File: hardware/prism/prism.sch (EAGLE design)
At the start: 136 parts, among them IC1 MAX3232CSE, IC2 XMEGA128-A1, IC3 LM1086CS-3.3, J1 1445055-2, J2 2MS1T2B4M6QNS, K1 LED_G, K2 LED_G, K3 LED_G, K4 LED_G, K5 LED_G, K6 LED_G, K7 LED_G, K8 LED_G, T1 FDFS2P753Z, T2 MMBT2222LT1G, T3 MMBT2222LT1G, T4 FDFS2P753Z, T5 MMBT2222LT1G, T6 MMBT2222LT1G, T7 FDFS2P753Z, T8 MMBT2222LT1G

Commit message: add 3,3v and 5v regulator
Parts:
- added C30: 1µF 25V, robotter_capacitor:1UFD_25V
- added C31: 10nF 50V, robotter_capacitor:10NF-F
- added C32: 100nF 50V, robotter_capacitor:100NF-F
- added C33, C34: 10µF 25V, robotter_capacitor:10UF-C_25V
- added D8: B160-13F, robotter_diode:B160-13F
- added IC4: LM25011MY, robotter_ic:LM25011MY
- added L1: SDR0805-270KL, robotter_inductor:SDR0805-270KL
- added R58: 75K-F, robotter_resistor:75K-F
- added R59: 100_1W-1W, robotter_resistor:100_1W-1W
- added R60: 10K-F, robotter_resistor:10K-F
- added R61: 3K09-F, robotter_resistor:3K09-F
- C19, C23, C25, C26: device rcl:C-EUC0805 -> robotter_capacitor:100NF-F
- C21: value C_10UF -> 10µF 25V; device robotter_capacitor:C_10UF -> robotter_capacitor:10UF-C_25V
- C22: value C_10UF -> 1µF 25V; device robotter_capacitor:C_10UF -> robotter_capacitor:1UFD_25V
- C28: value 10UFC -> 10UF-C_25V; device robotter_capacitor:10UFC -> robotter_capacitor:10UF-C_25V
- D7: value 50WQ03 -> (none)
- IC3: value LM1086CS-3.3 -> NCV78M05BDTRKG; device robotter_ic:LM1086CS-3.3 -> linear:NCV78M05BDTRKG
- R14: device robotter_resistor:RES_1K -> robotter_resistor:RES_2K2
- R22: value RES_0 -> 0.27-F; device robotter_resistor:RES_0 -> robotter_resistor:0.27-F
- R27, R31, R38, R45: device rcl:R-EU_R0603 -> robotter_resistor:1K-F
- RF: value YELLOW_0805 -> YELLOW
- T2, T3, T5, T6, T8: device transistor-neu-to92:MMBT2222ALT1-NPN-SOT23-BEC -> robotter_ic:MMBT2222ALT1-NPN-SOT23-BEC
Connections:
- removed net 3V3_BUS: R22.1
- new net N$38: C32.2, D8.C, IC4.SW, L1.1
- new net N$39: D8.A, IC4.CS, R22.2
- new net N$40: IC4.RT, R58.1
- new net N$41: C21.1, IC3.VI, R59.2
- new net N$43: C31.1, IC4.SS
- new net N$44: IC4.FB, R60.1, R61.2
- new net N$48: C32.1, IC4.BST
- net +3V3: now also C33.1, L1.2, R61.1; no longer C22.1, IC3.VOUT@0, IC3.VOUT@1, R22.2
- net +5V: now also C34.1, IC3.VO; no longer C21.1, IC3.VIN
- net GND: now also C30.2, C31.2, C33.2, C34.2, IC4.CSG, IC4.SGND, R22.1, R60.2
- net VBAT: now also C22.1, C30.1, IC4.VIN, R58.2, R59.1
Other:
- note removed: "manque regulo 5V"
- note removed: "vérifier puissance dissipée dans régulos"
- moved on the sheet: C21, C22, R22

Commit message: photointerrupter added to board, interfaces added, regulator added
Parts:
- removed D1, D4: bzv55-c3v3, diode:ZENER-DIODESOD80C
- removed MIRROR_IDX0, MIRROR_IDX1: 794681-4, con-amp:794681-4
- removed R19: nc, rcl:R-EU_R0603
- removed R20: 4k7, rcl:R-EU_R0805
- removed R36: nc, rcl:R-EU_R0805
- removed R47: 10k, rcl:R-EU_R0603
- removed T7: FDFS2P753Z, robotter:FDFS2P753Z
- added C35, C36, C37, C38, C39, C40: 100nF 50V, robotter_capacitor:100NF-F
- added IC5, IC6: 74LVC4245A, robotter_ic:74LVC4245A
- added PH1, PH2: GP1S58VJ000F, robotter_ic:GP1S58VJ000F
- added R62, R63: 10K-F, robotter_resistor:10K-F
- added R64: 4K7-E, robotter_resistor:4K7-E
- added R65, R66, R67, R68, R69, R70, R71: 0-F, robotter_resistor:0-F
- added T9: NTGS4111PT1G, robotter_ic:NTGS4111PT1G
- C1, C10, C11, C12, C13, C14, C15, C16, C3, C4, C5, C6, C7, C9: value C_10UF -> 100nF 50V; device robotter_capacitor:C_10UF -> robotter_capacitor:100NF-F
- C17, C18: value C_10UF -> 15pF_0603_100V; device robotter_capacitor:C_10UF -> robotter_capacitor:15PF-F
- C19, C23, C25, C26: value 100nF -> 100nF 50V
- C2: value 330UF_35V_G_EEEFK1V331P -> 330µF 35V; device robotter_capacitor:C_POL_330UF -> robotter_capacitor:330UF
- C20, C24: value 100nF -> 100nF 50V; device rcl:C-EUC0603 -> robotter_capacitor:100NF-F
- C27: value 10uF_35V_TANTALE -> 10µF 25V; device robotter_capacitor:C_POL_10UF -> robotter_capacitor:10UF-C_25V
- C28: value 10UF-C_25V -> 10µF 25V
- C29: value 100nF_0603_50V -> 100nF 50V
- C8: value C_10UF -> 10µF 25V; device robotter_capacitor:C_10UF -> robotter_capacitor:10UF-C_25V
- D2, D5: device diode:ZENER-DIODESOD80C -> robotter_diode:BZV55-C3V3SOD80C
- D3, D6: device diode:CGRM4004-G -> robotter_diode:CGRM4004-G
- IR_SENSOR0, IR_SENSOR1: device con-amp:794681-4 -> robotter_connector:794681-4
- R1, R2, R48, R49, R5, R6, R7, R8: value RES_15K -> 270-F; device robotter_resistor:RES_15K -> robotter_resistor:270-F
- R12: value nc -> 4K7-F; device rcl:R-EU_R0603 -> robotter_resistor:4K7-F
- R13: value 15K_5P_0805 -> 15k 1%; device robotter_resistor:RES_15K -> robotter_resistor:15K-E
- R14: value 1K_5P_0805 -> 1k; device robotter_resistor:RES_2K2 -> robotter_resistor:1K-E
- R15, R23, R24, R26, R3, R30, R32, R35, R37, R39, R4, R40, R46, R51, R52: value 10k -> 10K-F; device rcl:R-EU_R0603 -> robotter_resistor:10K-F
- R16: value 10k -> 4K7-F; device rcl:R-EU_R0603 -> robotter_resistor:4K7-F
- R17: value 4k7 -> 270-F; device rcl:R-EU_R0805 -> robotter_resistor:270-F
- R18: value nc -> 270-F; device rcl:R-EU_R0805 -> robotter_resistor:270-F
- R43: value 4k7 -> 4K7-E; device rcl:R-EU_R0805 -> robotter_resistor:4K7-E
- R44: value 4k7 -> 0-F; device rcl:R-EU_R0805 -> robotter_resistor:0-F
- T1, T4: value FDFS2P753Z -> NTGS4111PT1G; device robotter:FDFS2P753Z -> robotter_ic:NTGS4111PT1G
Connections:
- removed net INT1_5V: BAL0.6
- removed net MIRROR_1_INDEX_3V3: D4.C, R12.2, R43.1
- removed net MIRROR_INDEX_0_24V: MIRROR_IDX0.2, R16.1, R17.2, R18.2
- removed net MIRROR_INDEX_1_24V: MIRROR_IDX1.2, R36.2, R37.1, R43.2
- new net INT0_0_3V3: IC6.IO_VL5, R71.1
- new net INT0_1_3V3: IC6.IO_VL4, R70.1
- new net INT1_0_3V3: IC6.IO_VL3, R69.1
- new net INT1_0_5V: BAL0.6, IC5.IO_VCC3, R65.2
- new net INT1_1_3V3: IC6.IO_VL2, R68.1
- new net MIRROR_INDEX_1_3V3: PH2.TRANSISTOR_C, R12.1
- new net N$47: IC6.IO_VCC2, R44.1
- new net N$49: IC5.IO_VL2, R68.2
- new net N$50: IC5.IO_VL4, R70.2
- new net N$51: IC5.IO_VL3, R69.2
- new net N$52: IC5.IO_VL5, R71.2
- new net N$53: IC6.IO_VCC3, R65.1
- new net N$54: IC6.IO_VCC5, R67.1
- new net N$55: IC6.IO_VCC4, R66.1
- new net N$56: PH2.LED_A, R18.1
- new net N$57: PH1.LED_A, R17.1
- new net SYNC_IN_0_3V3: IC5.IO_VL6
- new net SYNC_IN_1_3V3: IC5.IO_VL7
- new net SYNC_OUT_0_3V3: IC6.IO_VL6
- new net SYNC_OUT_1_3V3: IC6.IO_VL7
- net +3V3: now also C19.1, C26.1, C27.1, C35.1, C37.1, C39.1, C40.1, C6.1, IC5.DIR_H_TO_L, IC5.VL@0, IC5.VL@1, IC6.VL@0, IC6.VL@1, R12.2, R16.2, R17.2, R18.2, R62.1, R63.1; no longer C1.1, C27.+
- net +5V: now also C36.1, C38.1, IC5.VCC, IC6.VCC
- net GND: now also C17.2, C18.2, C27.2, C3.2, C35.2, C36.2, C37.2, C38.2, C39.2, C40.2, C6.2, IC5./OE, IC5.GND@0, IC5.GND@1, IC5.GND@2, IC6./OE, IC6.DIR_H_TO_L, IC6.GND@0, IC6.GND@1, IC6.GND@2, PH1.LED_C, PH1.TRANSISTOR_E, PH2.LED_C, PH2.TRANSISTOR_E, R35.1, R37.1; no longer C17.1, C18.1, C27.-, C4.2, C5.2, D1.A, D4.A, MIRROR_IDX0.1, MIRROR_IDX1.1, R12.1, R18.1, R19.1, R36.1, R46.1, R47.1
- net INT0_0_5V: now also IC5.IO_VCC5, R67.2
- net INT0_1_5V: now also IC5.IO_VCC4, R66.2
- net INT1_1_5V: now also IC5.IO_VCC2, R44.2
- net IR_SENSOR_0_OUTPUT_24V: now also R23.1, R64.1; no longer R20.2, R24.1
- net IR_SENSOR_0_OUTPUT_3V3: now also R64.2; no longer R20.1
- net IR_SENSOR_1_OUTPUT_24V: now also R39.1, R43.1; no longer R35.1, R44.2
- net IR_SENSOR_1_OUTPUT_3V3: now also R43.2; no longer R44.1
- net MIRROR_INDEX_0_3V3: now also PH1.TRANSISTOR_C, R16.1; no longer D1.C, R17.1, R19.2
- net MOTOR_PWM_1_3V3: now also R37.2; no longer R46.2
- net N$1: now also C5.1; no longer C3.1
- net N$11: now also C1.1; no longer C4.1
- net N$125: now also R23.2, T1.D@0, T1.D@1, T1.D@2, T1.D@3; no longer R24.2, T1.D, T1.D1
- net N$128: now also R24.1; no longer R23.1
- net N$13: now also C3.1; no longer C5.1
- net N$14: now also R46.1; no longer R39.1
- net N$24: now also C4.2; no longer C6.2
- net N$26: now also R51.2, R52.1, T9.G; no longer R51.1, R52.2, T7.G
- net N$29: now also R51.1; no longer R52.1
- net N$30: now also R52.2, T9.S; no longer R51.2, T7.S
- net N$45: now also C17.1; no longer C17.2
- net N$46: now also C18.1; no longer C18.2
- net N$5: now also C5.2; no longer C3.2
- net N$6: now also C4.1; no longer C6.1
- net N$8: now also C25.1, R39.2, T4.D@0, T4.D@1, T4.D@2, T4.D@3; no longer C24.1, R35.2, T4.D, T4.D1
- net ON/OFF_SENSOR_1_3V3: now also R35.2; no longer R47.2
- net RX_1_3V3: now also R62.2
- net SYNC_IN_0_5V: now also IC5.IO_VCC6
- net SYNC_IN_1_5V: now also IC5.IO_VCC7
- net SYNC_OUT_0_5V: now also IC6.IO_VCC6
- net SYNC_OUT_1_5V: now also IC6.IO_VCC7
- net TX_1_3V3: now also R63.2
- net VBAT: now also C24.1, R24.2, R46.2, T9.D@0, T9.D@1, T9.D@2, T9.D@3; no longer C19.1, C25.1, C26.1, MIRROR_IDX0.3, MIRROR_IDX1.3, R16.2, R23.2, R37.2, R39.2, T7.D, T7.D1
- net XBEE_CTS_3V3: now also IC2.PH2(!RAS!/ALE1)
- net XBEE_RTS_3V3: now also IC2.PH3(!DOM!/ALE2)
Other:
- note added: "3v3 -> 5v"
- note added: "3v3 <- 5v"
- moved on the sheet: BAL0, BAL1, C1, C10, C11, C12, C13, C14, C15, C16, C17, C18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

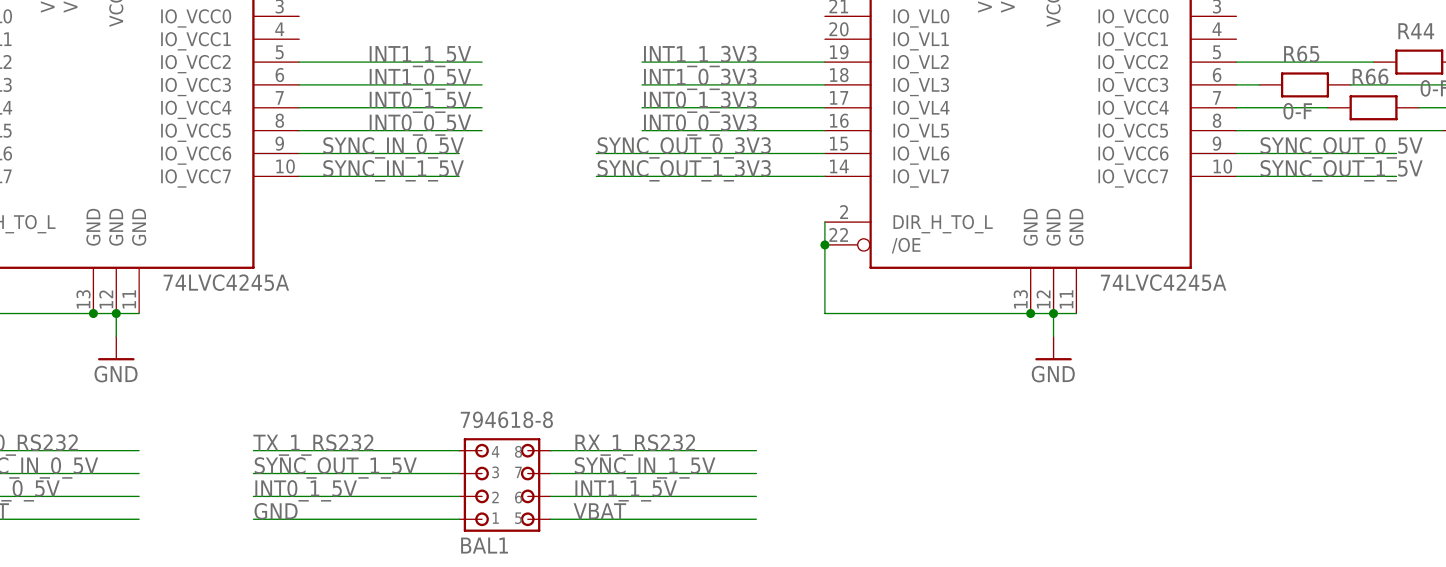
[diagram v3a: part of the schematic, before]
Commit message: prism/prism.brd
correction after Damien review
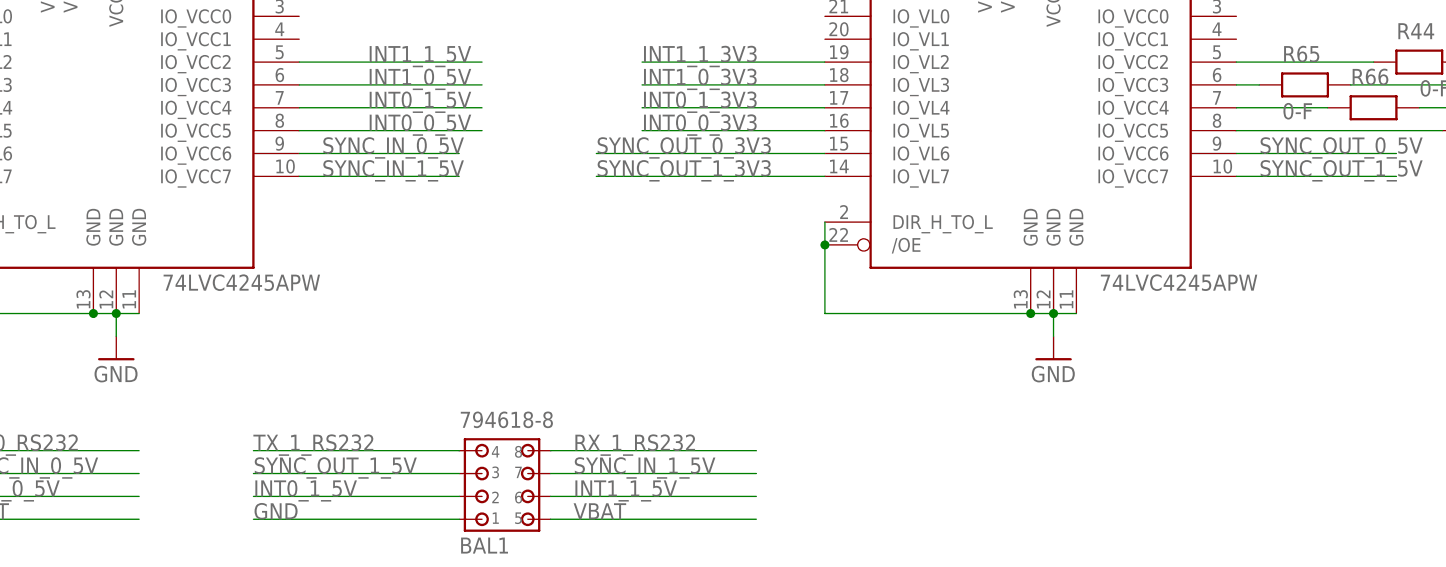
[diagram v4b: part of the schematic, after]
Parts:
- IC5, IC6: value 74LVC4245A -> 74LVC4245APW; device robotter_ic:74LVC4245A -> robotter_ic:74LVC4245APW
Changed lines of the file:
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@@
 <part name="R64" library="robotter_resistor" deviceset="4K7" device="-E"/>
 <part name="R43" library="robotter_resistor" deviceset="4K7" device="-E"/>
-<part name="IC6" library="robotter_ic" deviceset="74LVC4245" device="A"/>
+<part name="IC6" library="robotter_ic" deviceset="74LVC4245" device="APW"/>
 <part name="P+4" library="supply1" deviceset="+5V" device=""/>
 <part name="+3V5" library="supply1" deviceset="+3V3" device=""/>
@@
 <part name="R66" library="robotter_resistor" deviceset="0" device="-F"/>
 <part name="R67" library="robotter_resistor" deviceset="0" device="-F"/>
-<part name="IC5" library="robotter_ic" deviceset="74LVC4245" device="A"/>
+<part name="IC5" library="robotter_ic" deviceset="74LVC4245" device="APW"/>
 <part name="P+5" library="supply1" deviceset="+5V" device=""/>
 <part name="+3V7" library="supply1" deviceset="+3V3" device=""/>

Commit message: prism schematic modified, frist routing test
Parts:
- removed C26: 100nF 50V, robotter_capacitor:100NF-F
- removed H4: MOUNT-PAD-ROUND5.5, holes:MOUNT-PAD-ROUND5.5
- removed IR_SENSOR1: 794681-4, robotter_connector:794681-4
- removed PH2: GP1S58VJ000F, robotter_ic:GP1S58VJ000F
- removed R41: nc, rcl:R-EU_R0603
- removed R42: 0, rcl:R-EU_R0603
- removed R59: 100_1W-1W, robotter_resistor:100_1W-1W
- added C41: 180pF 50V, robotter_capacitor:180PF-F
- added C42, C43: 10µF 25V, robotter_capacitor:10UF-C_25V
- added D1: B120-13-F, robotter_diode:B120-13-F
- added IC7: LM2731XMF, robotter_ic:LM2731XMF
- added J3: 794618-4, robotter_connector:794618-4
- added L2: SRR7032-100M, robotter_inductor:SRR7032-100M
- added L3: 220 ohms, robotter_inductor:FERRITE_220OHMS
- added R19, R36: 10K_1%-F, robotter_resistor:10K_1%-F
- added R20: 113K-F, robotter_resistor:113K-F
- IR_SENSOR0: value 794681-4 -> 794618-4; device robotter_connector:794681-4 -> robotter_connector:794618-4
- PDI_ATMEL: device robotter_connector:PDI_ATMEL -> robotter_connector:PDI_ATMELL
- R12: value 4K7-F -> 0-F; device robotter_resistor:4K7-F -> robotter_resistor:0-F
- R18: value 270-F -> 0-F; device robotter_resistor:270-F -> robotter_resistor:0-F
- R50: value 10K-E -> 1K-F; device robotter_resistor:10K-E -> robotter_resistor:1K-F
- renumbered J1 to BATT, J2 to SW_BATT
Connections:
- removed net IR_SENSOR_OUTPUT_0_3V3: IC2.PC2(OC0C/RXD0)
- removed net IR_SENSOR_OUTPUT_1_3V3: IC2.PE2(OC0C/RXD0)
- removed net MIRROR_INDEX_10_3V3: IC2.PE3(OC0D/TXD0)
- removed net N$125: C20.1, IR_SENSOR0.3, R23.2, R25.2, T1.D@0, T1.D@1, T1.D@2, T1.D@3
- removed net N$15: IR_SENSOR1.4, R41.2, R42.1
- new net +15V: C20.1, C25.1, C41.1, C42.1, D1.C, R20.1, R24.2, R46.2, T1.S, T4.S
- new net N$58: J3.3, R12.2, R39.2, T4.D@0, T4.D@1, T4.D@2, T4.D@3
- new net N$59: D1.A, IC7.SW, L2.2
- new net N$60: C41.2, IC7.FB, R19.2, R20.2
- new net N$63: IC7./SHDN, R36.1
- net +3V3: now also L3.2; no longer C26.1, C7.1, C8.1, IC2.AVCC-A, IC2.AVCC-B, R12.2, R18.2
- net GND: now also C42.2, C43.2, IC7.GND, J3.1, R18.1, R19.1; no longer C26.2, H4.MOUNT, IR_SENSOR1.1, PH2.LED_C, PH2.TRANSISTOR_E, R41.1
- net IR_SENSOR_0_OUTPUT_3V3: now also IC2.PC2(OC0C/RXD0)
- net IR_SENSOR_1_OUTPUT_24V: now also J3.2; no longer IR_SENSOR1.2
- net IR_SENSOR_1_OUTPUT_3V3: now also IC2.PE2(OC0C/RXD0)
- net MIRROR_INDEX_1_3V3: now also IC2.PE3(OC0D/TXD0); no longer PH2.TRANSISTOR_C, R12.1
- net N$41: now also J3.4, R12.1, R18.2; no longer C21.1, IC3.VI, R59.2
- net N$56: now also IR_SENSOR0.3, R23.2, R25.2, T1.D@0, T1.D@1, T1.D@2, T1.D@3; no longer PH2.LED_A, R18.1
- net N$8: now also C7.1, C8.1, IC2.AVCC-A, IC2.AVCC-B, L3.1; no longer C25.1, IR_SENSOR1.3, R39.2, R42.2, T4.D@0, T4.D@1, T4.D@2, T4.D@3
- net SYNC_IN_0_3V3: now also IC2.PC4(OC1A/!SS!)
- net SYNC_IN_1_3V3: now also IC2.PC5(OC1B/MOSI/XCK1)
- net SYNC_OUT_0_3V3: now also IC2.PC6(MISO/RXD1)
- net SYNC_OUT_1_3V3: now also IC2.PC7(SCK/TXD1/CLKO/EVO)
- net VBAT: now also C21.1, C43.1, IC3.VI, IC7.VIN, L2.1, R36.2; no longer R24.2, R46.2, R59.1, T1.S, T4.S
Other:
- note added: "connect 2s lipo batterie ( 6.6-8.4V)"
- moved on the sheet: C20, C21, C22, C25, C30, C31, C32, C33, C34, C40, C7, C8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

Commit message: added bluetooth board, begining of routing
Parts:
- removed BAL0: 794618-8, robotter_connector:794618-8
- removed D8: B160-13F, robotter_diode:B160-13F
- removed IR_SENSOR0, J3: 794618-4, robotter_connector:794618-4
- removed K1, K2, K3, K4: LED_G, robotter_diode:LED_G
- removed PH1: GP1S58VJ000F, robotter_ic:GP1S58VJ000F
- removed SYNC0: LED_B, robotter_diode:LED_B
- removed T9: NTGS4111PT1G, robotter_ic:NTGS4111PT1G
- added BAL2: 794618-8, robotter_connector:794618-8
- added C26: 1µF 25V, robotter_capacitor:1UFD_25V
- added C44: 100nF 50V, robotter_capacitor:100NF-F
- added D4: bzv55-c3v3, robotter_diode:BZV55-C3V3SOD80C
- added IC8: MAX3232CSE, robotter_ic:MAX3232CSE
- added IDX0: PRISM_INDEX_EXTENSION_MALE, robotter_others:PRISM_INDEX_EXTENSION_MALE
- added IDX1: GP1S58VJ000F, robotter_ic:GP1S58VJ000F
- added IR_SENS0: 794681-4, robotter_connector:794681-4
- added IR_SENSOR1: 794618-4, robotter_connector:794618-4
- added LIDX0, LIDX1, LK4, LK5: LED_G, robotter_diode:LED_G
- added R41: nc, rcl:R-EU_R0603
- added R42, R72: 10K-F, robotter_resistor:10K-F
- added R47, R59: 270-F, robotter_resistor:270-F
- added R73: 0-F, robotter_resistor:0-F
- added SYNC2: LED_B, robotter_diode:LED_B
- added T7: MMBT2222LT1G, robotter_ic:MMBT2222ALT1-NPN-SOT23-BEC
- C1: value 100nF 50V -> 15pF_0603_100V; device robotter_capacitor:100NF-F -> robotter_capacitor:15PF-F
- C15, C20, C32, C37: value 100nF 50V -> 10µF 25V; device robotter_capacitor:100NF-F -> robotter_capacitor:10UF-C_25V
- C17, C18: value 15pF_0603_100V -> 100nF 50V; device robotter_capacitor:15PF-F -> robotter_capacitor:100NF-F
- C2: value 330µF 35V -> 15pF_0603_100V; device robotter_capacitor:330UF -> robotter_capacitor:15PF-F
- C22, C30: value 1µF 25V -> 100nF 50V; device robotter_capacitor:1UFD_25V -> robotter_capacitor:100NF-F
- C24: value 100nF 50V -> 330µF 35V; device robotter_capacitor:100NF-F -> robotter_capacitor:330UF
- C29: value 100nF 50V -> 1µF 25V; device robotter_capacitor:100NF-F -> robotter_capacitor:1UFD_25V
- C31: value 10nF 50V -> 100nF 50V; device robotter_capacitor:10NF-F -> robotter_capacitor:100NF-F
- C33: value 10µF 25V -> 10nF 50V; device robotter_capacitor:10UF-C_25V -> robotter_capacitor:10NF-F
- C34, C42, C8: value 10µF 25V -> 100nF 50V; device robotter_capacitor:10UF-C_25V -> robotter_capacitor:100NF-F
- C40: value 100nF 50V -> 180pF 50V; device robotter_capacitor:100NF-F -> robotter_capacitor:180PF-F
- C41: value 180pF 50V -> 10µF 25V; device robotter_capacitor:180PF-F -> robotter_capacitor:10UF-C_25V
- D1: value B120-13-F -> CGRM4004-G; device robotter_diode:B120-13-F -> robotter_diode:CGRM4004-G
- D2: value bzv55-c3v3 -> CGRM4004-G; device robotter_diode:BZV55-C3V3SOD80C -> robotter_diode:CGRM4004-G
- D3: value CGRM4004-G -> bzv55-c3v3; device robotter_diode:CGRM4004-G -> robotter_diode:BZV55-C3V3SOD80C
- D5: value bzv55-c3v3 -> (none); device robotter_diode:BZV55-C3V3SOD80C -> robotter_diode:50WQ03
- D6: value CGRM4004-G -> B120-13-F; device robotter_diode:CGRM4004-G -> robotter_diode:B120-13-F
- D7: value (none) -> B160-13F; device robotter_diode:50WQ03 -> robotter_diode:B160-13F
- IC1: value MAX3232CSE -> XMEGA128-A1; device robotter_ic:MAX3232CSE -> avr-7:XMEGA-A1TQFP
- IC2: value XMEGA128-A1 -> 74LVC4245APW; device avr-7:XMEGA-A1TQFP -> robotter_ic:74LVC4245APW
- IC3: value NCV78M05BDTRKG -> LM2731XMF; device linear:NCV78M05BDTRKG -> robotter_ic:LM2731XMF
- IC4: value LM25011MY -> 74LVC4245APW; device robotter_ic:LM25011MY -> robotter_ic:74LVC4245APW
- IC5: value 74LVC4245APW -> LM25011MY; device robotter_ic:74LVC4245APW -> robotter_ic:LM25011MY
- IC6: value 74LVC4245APW -> NCV78M05BDTRKG; device robotter_ic:74LVC4245APW -> linear:NCV78M05BDTRKG
- IC7: value LM2731XMF -> NRF24L01+; device robotter_ic:LM2731XMF -> robotter_ic:NRF24L01+
- L1: value SDR0805-270KL -> 220 ohms; device robotter_inductor:SDR0805-270KL -> robotter_inductor:FERRITE_220OHMS
- L3: value 220 ohms -> SDR0805-270KL; device robotter_inductor:FERRITE_220OHMS -> robotter_inductor:SDR0805-270KL
- R1, R2: value 270-F -> 0-E; device robotter_resistor:270-F -> robotter_resistor:0-E
- R10, R11, R5, R54, R55, R7, R9: value 270-F -> 10K-F; device robotter_resistor:270-F -> robotter_resistor:10K-F
- R12: value 0-F -> 1k; device robotter_resistor:0-F -> robotter_resistor:1K-F
- R13: value 15k 1% -> 10K-F; device robotter_resistor:15K-E -> robotter_resistor:10K-F
- R14: value 1k -> 10K-F; device robotter_resistor:1K-E -> robotter_resistor:10K-F
- R16: value 4K7-F -> 1k; device robotter_resistor:4K7-F -> robotter_resistor:1K-F
- R18: value 0-F -> 0; device robotter_resistor:0-F -> rcl:R-EU_R0603
- R19, R36: value 10K_1%-F -> nc; device robotter_resistor:10K_1%-F -> rcl:R-EU_R0603
- R20: value 113K-F -> 10K-F; device robotter_resistor:113K-F -> robotter_resistor:10K-F
- R22: value 0.27-F -> 0-F; device robotter_resistor:0.27-F -> robotter_resistor:0-F
- R23: value 10K-F -> 0-F; device robotter_resistor:10K-F -> robotter_resistor:0-F
- R24: value 10K-F -> 4K7-F; device robotter_resistor:10K-F -> robotter_resistor:4K7-F
- R25: value 0 -> 270-F; device rcl:R-EU_R0603 -> robotter_resistor:270-F
- R27: value 1k -> nc; device robotter_resistor:1K-F -> rcl:R-EU_R0603
- R28: value nc -> 270-F; device rcl:R-EU_R0603 -> robotter_resistor:270-F
- R29, R34: value nc -> 4K7-E; device rcl:R-EU_R0603 -> robotter_resistor:4K7-E
- R31, R38: value 1k -> 270-F; device robotter_resistor:1K-F -> robotter_resistor:270-F
- R32, R35, R40, R52: value 10K-F -> 270-F; device robotter_resistor:10K-F -> robotter_resistor:270-F
- R33: value nc -> 10K-F; device rcl:R-EU_R0603 -> robotter_resistor:10K-F
- R4: value 10K-F -> 0-E; device robotter_resistor:10K-F -> robotter_resistor:0-E
- R43: value 4K7-E -> 10K-F; device robotter_resistor:4K7-E -> robotter_resistor:10K-F
- R45: value 1k -> 0-F; device robotter_resistor:1K-F -> robotter_resistor:0-F
- R46: value 10K-F -> 10K-E; device robotter_resistor:10K-F -> robotter_resistor:10K-E
- R49: value 270-F -> 0-F; device robotter_resistor:270-F -> robotter_resistor:0-F
- R50: value 1K-F -> 0-F; device robotter_resistor:1K-F -> robotter_resistor:0-F
- R51: value 10K-F -> 1K-F; device robotter_resistor:10K-F -> robotter_resistor:1K-F
- R53: value 10K-E -> 270-F; device robotter_resistor:10K-E -> robotter_resistor:270-F
- R58: value 75K-F -> 270-F; device robotter_resistor:75K-F -> robotter_resistor:270-F
- R6, R8: value 270-F -> 1k; device robotter_resistor:270-F -> robotter_resistor:1K-F
- R60: value 10K-F -> 15k 1%; device robotter_resistor:10K-F -> robotter_resistor:15K-E
- R61: value 3K09-F -> 1k; device robotter_resistor:3K09-F -> robotter_resistor:1K-E
- R62: value 10K-F -> 10K_1%-F; device robotter_resistor:10K-F -> robotter_resistor:10K_1%-F
- R63: value 10K-F -> 75K-F; device robotter_resistor:10K-F -> robotter_resistor:75K-F
- R64: value 4K7-E -> 0.27-F; device robotter_resistor:4K7-E -> robotter_resistor:0.27-F
- R65: value 0-F -> 113K-F; device robotter_resistor:0-F -> robotter_resistor:113K-F
- R66: value 0-F -> 10K_1%-F; device robotter_resistor:0-F -> robotter_resistor:10K_1%-F
- R67: value 0-F -> 10K-F; device robotter_resistor:0-F -> robotter_resistor:10K-F
- R71: value 0-F -> 3K09-F; device robotter_resistor:0-F -> robotter_resistor:3K09-F
- T1, T4: value NTGS4111PT1G -> MMBT2222LT1G; device robotter_ic:NTGS4111PT1G -> robotter_ic:MMBT2222ALT1-NPN-SOT23-BEC
- T2, T5, T8: value MMBT2222LT1G -> NTGS4111PT1G; device robotter_ic:MMBT2222ALT1-NPN-SOT23-BEC -> robotter_ic:NTGS4111PT1G
- renumbered K5 to LK0, K6 to LK1, K7 to LK2, K8 to LK3
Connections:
- removed net LED_SOUTH: IC2.PJ3(D3/A3/A11), R49.1, R8.1
- removed net N$21: LK2.A, R48.2
- removed net N$93: K3.A, R7.2
- removed net XBEE_CTS_3V3: IC2.PH2(!RAS!/ALE1), XB1.!CTS!/DIO7
- removed net XBEE_RTS_3V3: IC2.PH3(!DOM!/ALE2), XB1.!RTS!/AD6/DIO6
- removed net XBEE_RX_3V3: IC2.PD6(RXD1/MISO), XB1.DOUT
- removed net XBEE_TX_3V3: IC2.PD7(TXD1/SCK/CLKO/EVO), XB1.DIN/!CONFIG
- new net BEACON_ID_0_3V3: IC1.PB0(ADCB0/AREFB), R1.2
- new net BEACON_ID_1_3V3: IC1.PB1(ADCB1), R2.2
- new net BEACON_ID_2_3V3: IC1.PB2(ADCB2/DAC0), R4.2
- new net LED_INDEX_0_3V3: IC1.PK6(A6/A14/A22), R57.1
- new net LED_INDEX_1_3V3: IC1.PK7(A7/A15/A23), R59.1
- new net LK0_3V3: IC1.PK0(A0/A8/A16), R47.1
- new net LK1: LK2.A, R56.2
- new net LK1_3V3: IC1.PK1(A1/A9/A17), R52.1
- new net LK2_3V3: IC1.PK2(A2/A10/A18), R56.1
- new net LK3_3V3: IC1.PK3(A3/A11/A19), R58.1
- new net LK4_3V3: IC1.PK4(A4/A12/A20), R48.1
- new net LK5: LIDX0.A, R57.2
- new net LK5_3V3: IC1.PK5(A5/A13/A22), R53.1
- new net NRF_CSN_3V3: IC1.PE0(OC0A/SDA), IC7.CSN, R67.1
- new net NRF_MOSI_3V3: IC1.PD5(OC1B/XCK1/MOSI), IC7.MOSI
- new net XBEE_CTS_3V3/NRF_IRQ_3V3: IC1.PH2(!RAS!/ALE1), IC7.IRQ, XB1.!CTS!/DIO7
- new net XBEE_RTS_3V3/NRF_CE_3V3: IC1.PH3(!DOM!/ALE2), IC7.CE, XB1.!RTS!/AD6/DIO6
- new net XBEE_RX_3V3/NRF_MISO_3V3: IC1.PD6(RXD1/MISO), IC7.MISO, R43.2, XB1.DOUT
- new net XBEE_TX_3V3/NRF_SCK_3V3: IC1.PD7(TXD1/SCK/CLKO/EVO), IC7.SCK, R42.2, XB1.DIN/!CONFIG
- net +15V: now also C3.1, C4.1, C40.1, D6.C, R14.2, R65.1, R9.2, T2.S, T5.S; no longer C20.1, C25.1, C42.1, D1.C, R20.1, R24.2, R46.2, T1.S, T4.S
- net +3V3: now also C17.1, C18.1, C20.1, C21.1, C22.1, C23.1, C30.1, C31.1, C43.1, C5.1, C8.1, IC1.VCC@1, IC1.VCC@2, IC1.VCC@3, IC1.VCC@4, IC1.VCC@5, IC1.VCC@6, IC1.VCC@7, IC1.VCC@8, IC2.DIR_H_TO_L, IC2.VL@0, IC2.VL@1, IC4.VL@0, IC4.VL@1, IC7.+3V3, IC8P.VCC, IDX0.3V3, R24.2, R3.1, R30.1, R33.1, R37.2, R39.2, R67.2, R71.1; no longer C10.1, C15.1, C28.1, C29.1, C33.1, C35.1, C37.1, C40.1, C6.1, IC1P.VCC, IC2.VCC@1, IC2.VCC@2, IC2.VCC@3, IC2.VCC@4, IC2.VCC@5, IC2.VCC@6, IC2.VCC@7, IC2.VCC@8, IC5.DIR_H_TO_L, IC5.VL@0, IC5.VL@1, IC6.VL@0, IC6.VL@1, R15.1, R16.2, R3.2, R4.2, R61.1, R62.1, R63.1
- net +5V: now also C25.1, C37.1, IC2.VCC, IC4.VCC, IC6.VO; no longer C34.1, C36.1, IC3.VO, IC5.VCC, IC6.VCC
- net /RESET_3V3: now also IC1.PDI-CLK/!RESET, R3.2; no longer IC2.PDI-CLK/!RESET, R15.2
- net BATTERY_MONITOR_0-1V: now also IC1.PA2(ADCA2), R60.1, R61.2; no longer IC2.PA2(ADCA2), R13.1, R14.2
- net GND: now also BAL2.1, C2.2, C24.-, C26.2, C32.2, C4.2, C41.2, C5.2, D3.A, D4.A, IC1.GND@1, IC1.GND@10, IC1.GND@2, IC1.GND@3, IC1.GND@4, IC1.GND@5, IC1.GND@6, IC1.GND@7, IC1.GND@8, IC1.GND@9, IC2./OE, IC2.GND@0, IC4./OE, IC4.DIR_H_TO_L, IC4.GND@0, IC4.GND@1, IC4.GND@2, IC5.CSG, IC5.SGND, IC6.GND, IC8P.GND, IDX0.GND@0, IDX0.GND@1, IDX1.LED_C, IDX1.TRANSISTOR_E, IR_SENS0.1, IR_SENSOR1.1, LIDX0.C, LIDX1.C, LK4.C, LK5.C, R1.1, R11.1, R13.1, R2.1, R23.1, R27.1, R36.1, R4.1, R41.1, R42.1, R43.1, R46.1, R5.1, R61.1, R64.1, R66.1, R7.1, R72.2, SYNC2.C, T1.E, T4.E, T7.E; no longer BAL0.1, C2.-, C24.2, C36.2, C40.2, C42.2, D2.A, D5.A, IC1P.GND, IC2.GND@10, IC2.GND@3, IC2.GND@4, IC2.GND@5, IC2.GND@6, IC2.GND@7, IC2.GND@8, IC2.GND@9, IC4.CSG, IC4.SGND, IC5./OE, IC5.GND@0, IC5.GND@1, IC5.GND@2, IC6./OE, IC6.DIR_H_TO_L, IC6.GND@0, IC6.GND@1, IC6.GND@2, IR_SENSOR0.1, J3.1, K1.C, K2.C, K3.C, K4.C, PH1.LED_C, PH1.TRANSISTOR_E, R14.1, R18.1, R22.1, R28.1, R29.1, R30.1, R32.1, R33.1, R34.1, R35.1, R37.1, R53.1, R60.2, SYNC0.C, T2.E, T5.E, T8.E
- net INT0_0_3V3: now also IC4.IO_VL5, R50.1; no longer IC6.IO_VL5, R71.1
- net INT0_0_5V: now also BAL1.2, IC2.IO_VCC5, R73.2; no longer BAL0.2, IC5.IO_VCC5, R67.2
- net INT0_1_3V3: now also IC4.IO_VL4, R45.1; no longer IC6.IO_VL4, R70.1
- net INT0_1_5V: now also BAL2.2, IC2.IO_VCC4, R69.2; no longer BAL1.2, IC5.IO_VCC4, R66.2
- net INT1_0_3V3: now also IC4.IO_VL3, R49.1; no longer IC6.IO_VL3, R69.1
- net INT1_0_5V: now also BAL1.6, IC2.IO_VCC3, R68.2; no longer BAL0.6, IC5.IO_VCC3, R65.2
- net INT1_1_3V3: now also IC4.IO_VL2, R44.1; no longer IC6.IO_VL2, R68.1
- net INT1_1_5V: now also BAL2.6, IC2.IO_VCC2, R70.2; no longer BAL1.6, IC5.IO_VCC2, R44.2
- net IR_SENSOR_0_OUTPUT_24V: now also IR_SENSOR1.2, R20.1, R21.2, R34.1; no longer IR_SENSOR0.2, R23.1, R28.2, R64.1
- net IR_SENSOR_0_OUTPUT_3V3: now also D3.C, IC1.PC2(OC0C/RXD0), R29.2, R36.2; no longer D2.C, IC2.PC2(OC0C/RXD0), R21.2, R64.2
- net IR_SENSOR_1_OUTPUT_24V: now also IR_SENS0.2, R26.1, R27.2, R29.1; no longer J3.2, R34.2, R39.1, R43.1
- net IR_SENSOR_1_OUTPUT_3V3: now also D4.C, IC1.PE2(OC0C/RXD0), R34.2, R41.2; no longer D5.C, IC2.PE2(OC0C/RXD0), R33.2, R43.2
- net LED_EAST: now also IC1.PH1(!CAS!/!RE!); no longer IC2.PH1(!CAS!/!RE!), R2.1, R6.1
- net LED_NORTH: now also IC1.PH7(CLK/!CS3!/A19); no longer IC2.PH7(CLK/!CS3!/A19), R1.1, R5.1
- net LED_WEST: now also IC1.PA0(ADCA0/AREFA); no longer IC2.PA0(ADCA0/AREFA), R48.1, R7.1
- net MIRROR_INDEX_0_3V3: now also IC1.PC3(OC0D/TXD0), IDX0.IDX_3V3; no longer IC2.PC3(OC0D/TXD0), PH1.TRANSISTOR_C, R16.1
- net MIRROR_INDEX_1_3V3: now also IC1.PE3(OC0D/TXD0), IDX1.TRANSISTOR_C, R24.1; no longer IC2.PE3(OC0D/TXD0)
- net MOTOR_M_0: now also D2.A, T6.C; no longer D3.A, T3.C
- net MOTOR_M_1: now also D1.A, T4.C; no longer D6.A, T6.C
- net MOTOR_PWM_0_3V3: now also IC1.PD0(OC0A/SDA), R13.2, R16.1; no longer IC2.PD0(OC0A/SDA), R31.1, R32.2
- net MOTOR_PWM_1_3V3: now also IC1.PD1(OC0B/XCK0/SCL), R11.2, R12.1; no longer IC2.PD1(OC0B/XCK0/SCL), R37.2, R45.1
- net N$1: now also C44.1, IC8G$1.C1+; no longer C5.1, IC1G$1.C1+
- net N$10: now also IC1.PJ6(A10/D6/A6/A14), R31.1; no longer IC2.PK1(A1/A9/A17), R10.1
- net N$11: now also C34.1, IC8G$1.V+; no longer C1.1, IC1G$1.V+
- net N$12: now also IC1.PJ7(A11/D7/A7/A15), R35.1; no longer IC2.PK2(A2/A10/A18), R11.1
- net N$128: now also R10.2, R9.1, T2.G; no longer R24.1, R26.2, T1.G
- net N$129: now also IR_SENSOR1.4, R18.1, R19.2; no longer IR_SENSOR0.4, R25.1, R29.2
- net N$13: now also C35.1, IC8G$1.V-; no longer C3.1, IC1G$1.V-
- net N$14: now also R14.1, R15.2, T5.G; no longer R40.2, R46.1, T4.G
- net N$16: now also R8.2, T3.B; no longer R38.2, T5.B
- net N$17: now also R15.1, T3.C; no longer R40.1, T5.C
- net N$18: now also R16.2; no longer R45.2
- net N$19: now also R47.2; no longer R1.2
- net N$2: now also R25.2; no longer R9.2
- net N$20: now also R52.2; no longer R2.2
- net N$22: now also R58.2; no longer R49.2
- net N$23: now also D5.A1, D5.A2, SW_BATT.1; no longer D7.A1, D7.A2, SW_BATT.2
- net N$24: now also C42.2, IC8G$1.C2-; no longer C4.2, IC1G$1.C2-
- net N$25: now also R51.2, T7.B; no longer R50.2, T8.B
- net N$26: now also R54.1, R55.2, T8.G; no longer R51.2, R52.1, T9.G
- net N$27: now also R28.2; no longer R54.2
- net N$28: now also IC1.PJ0(D0/A0/A8), R28.1; no longer IC2.PJ4(A8/D4/A4/A12), R54.1
- net N$29: now also R55.1, T7.C; no longer R51.1, T8.C
- net N$3: now also R12.2, T4.B; no longer R31.2, T3.B
- net N$30: now also D5.C, R54.2, T8.S; no longer D7.C, R52.2, T9.S
- net N$31: now also IC1.PJ2(D2/A2/A10), R38.2; no longer IC2.PJ6(A10/D6/A6/A14), R55.2
- net N$32: now also IC1.PJ3(D3/A3/A11), R40.1; no longer IC2.PJ7(A11/D7/A7/A15), R56.1
- net N$33: now also R38.1, SYNC2.A; no longer R55.1, SYNC1.A
- net N$34: now also R40.2; no longer R56.2
- net N$35: now also R32.1, SYNC1.A; no longer R57.1, SYNC0.A
- net N$36: now also IC1.PJ1(D1/A1/A9), R32.2; no longer IC2.PJ5(A9/D5/A5/A13), R57.2
- net N$37: now also R6.2, T1.B; no longer R27.2, T2.B
- net N$38: now also C36.2, D7.C, IC5.SW, L3.1; no longer C32.2, D8.C, IC4.SW, L1.1
- net N$39: now also D7.A, IC5.CS, R64.2; no longer D8.A, IC4.CS, R22.2
- net N$4: now also R31.2; no longer R10.2
- net N$40: now also IC5.RT, R63.1; no longer IC4.RT, R58.1
- net N$41: now also IR_SENS0.4, R22.1, R23.2; no longer J3.4, R12.1, R18.2
- net N$42: now also R10.1, T1.C; no longer R26.1, T2.C
- net N$43: now also C33.1, IC5.SS; no longer C31.1, IC4.SS
- net N$44: now also IC5.FB, R71.2, R72.1; no longer IC4.FB, R60.1, R61.2
- net N$45: now also C1.1, IC1.PR0(XTAL2); no longer C17.1, IC2.PR0(XTAL2)
- net N$46: now also C2.1, IC1.PR1(XTAL1); no longer C18.1, IC2.PR1(XTAL1)
- net N$47: now also IC4.IO_VCC2, R70.1; no longer IC6.IO_VCC2, R44.1
- net N$48: now also C36.1, IC5.BST; no longer C32.1, IC4.BST
- net N$49: now also IC2.IO_VL2, R44.2; no longer IC5.IO_VL2, R68.2
- net N$5: now also C44.2, IC8G$1.C1-; no longer C5.2, IC1G$1.C1-
- net N$50: now also IC2.IO_VL4, R45.2; no longer IC5.IO_VL4, R70.2
- net N$51: now also IC2.IO_VL3, R49.2; no longer IC5.IO_VL3, R69.2
- net N$52: now also IC2.IO_VL5, R50.2; no longer IC5.IO_VL5, R71.2
- net N$53: now also IC4.IO_VCC3, R68.1; no longer IC6.IO_VCC3, R65.1
- net N$54: now also IC4.IO_VCC5, R73.1; no longer IC6.IO_VCC5, R67.1
- net N$55: now also IC4.IO_VCC4, R69.1; no longer IC6.IO_VCC4, R66.1
- net N$56: now also IR_SENSOR1.3, R18.2, R20.2, T2.D@0, T2.D@1, T2.D@2, T2.D@3; no longer IR_SENSOR0.3, R23.2, R25.2, T1.D@0, T1.D@1, T1.D@2, T1.D@3
- net N$57: now also IDX1.LED_A; no longer PH1.LED_A
- net N$58: now also IR_SENS0.3, R22.2, R26.2, T5.D@0, T5.D@1, T5.D@2, T5.D@3; no longer J3.3, R12.2, R39.2, T4.D@0, T4.D@1, T4.D@2, T4.D@3
- net N$59: now also D6.A, IC3.SW; no longer D1.A, IC7.SW
- net N$6: now also C42.1, IC8G$1.C2+; no longer C4.1, IC1G$1.C2+
- net N$60: now also C40.2, IC3.FB, R65.2, R66.2; no longer C41.2, IC7.FB, R19.2, R20.2
- net N$63: now also IC3./SHDN, R62.1; no longer IC7./SHDN, R36.1
- net N$7: now also R35.2; no longer R11.2
- net N$8: now also C10.1, C15.1, IC1.AVCC-A, IC1.AVCC-B, L1.1; no longer C7.1, C8.1, IC2.AVCC-A, IC2.AVCC-B, L3.1
- net N$9: now also IC1.PJ5(A9/D5/A5/A13), R25.1; no longer IC2.PK0(A0/A8/A16), R9.1
- net N$91: now also LK4.A, R48.2; no longer K1.A, R5.2
- net N$92: now also LK5.A, R53.2; no longer K2.A, R6.2
- net N$94: now also LIDX1.A, R59.2; no longer K4.A, R8.2
- net ON/OFF_SENSOR_0_3V3: now also IC1.PD2(OC0C/RXD0), R7.2, R8.1; no longer IC2.PD3(OC0D/TXD0), R27.1, R30.2
- net ON/OFF_SENSOR_1_3V1: now also R46.2, R51.1, SW_BATT.3; no longer R50.1, R53.2, SW_BATT.1
- net ON/OFF_SENSOR_1_3V3: now also IC1.PD3(OC0D/TXD0), R5.2, R6.1; no longer IC2.PD4(OC1A/!SS!), R35.2, R38.1
- net PDI_DATA_3V3: now also IC1.PDI-DATA; no longer IC2.PDI-DATA
- net RX_0_3V3: now also IC1.PF6(RXD1/MISO), IC8G$1.R1OUT, R37.1; no longer IC1G$1.R1OUT, IC2.PF6(RXD1/MISO), R3.1
- net RX_0_RS232: now also BAL1.8, IC8G$1.R1IN; no longer BAL0.8, IC1G$1.R1IN
- net RX_1_3V3: now also IC1.PF2(OC0C/RXD0), IC8G$1.R2OUT, R30.2; no longer IC1G$1.R2OUT, IC2.PF2(OC0C/RXD0), R62.2
- net RX_1_RS232: now also BAL2.8, IC8G$1.R2IN; no longer BAL1.8, IC1G$1.R2IN
- net SYNC_IN_0_3V3: now also IC1.PC4(OC1A/!SS!), IC2.IO_VL6; no longer IC2.PC4(OC1A/!SS!), IC5.IO_VL6
- net SYNC_IN_0_5V: now also BAL1.7, IC2.IO_VCC6; no longer BAL0.7, IC5.IO_VCC6
- net SYNC_IN_1_3V3: now also IC1.PC5(OC1B/MOSI/XCK1), IC2.IO_VL7; no longer IC2.PC5(OC1B/MOSI/XCK1), IC5.IO_VL7
- net SYNC_IN_1_5V: now also BAL2.7, IC2.IO_VCC7; no longer BAL1.7, IC5.IO_VCC7
- net SYNC_OUT_0_3V3: now also IC1.PC6(MISO/RXD1), IC4.IO_VL6; no longer IC2.PC6(MISO/RXD1), IC6.IO_VL6
- net SYNC_OUT_0_5V: now also BAL1.3, IC4.IO_VCC6; no longer BAL0.3, IC6.IO_VCC6
- net SYNC_OUT_1_3V3: now also IC1.PC7(SCK/TXD1/CLKO/EVO), IC4.IO_VL7; no longer IC2.PC7(SCK/TXD1/CLKO/EVO), IC6.IO_VL7
- net SYNC_OUT_1_5V: now also BAL2.3, IC4.IO_VCC7; no longer BAL1.3, IC6.IO_VCC7
- net TX_0_3V3: now also IC1.PF7(TXD1/SCK), IC8G$1.T1IN, R39.1; no longer IC1G$1.T1IN, IC2.PF7(TXD1/SCK), R4.1
- net TX_0_RS232: now also BAL1.4, IC8G$1.T1OUT; no longer BAL0.4, IC1G$1.T1OUT
- net TX_1_3V3: now also IC1.PF3(OC0D/TXD0), IC8G$1.T2IN, R33.2; no longer IC1G$1.T2IN, IC2.PF3(OC0D/TXD0), R63.2
- net TX_1_RS232: now also BAL2.4, IC8G$1.T2OUT; no longer BAL1.4, IC1G$1.T2OUT
- net VBAT: now also BAL2.5, C24.+, C26.1, C28.1, C29.1, C32.1, C6.1, C7.1, D1.C, D2.C, IC3.VIN, IC5.VIN, IC6.VI, R60.2, R62.2, R63.2, T8.D@0, T8.D@1, T8.D@2, T8.D@3; no longer BAL0.5, C2.+, C21.1, C22.1, C23.1, C24.1, C30.1, C43.1, D3.C, D6.C, IC3.VI, IC4.VIN, IC7.VIN, R13.2, R36.2, R58.2, T9.D@0, T9.D@1, T9.D@2, T9.D@3
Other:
- note added: "SW_BATT is a switch used to drive the mos that cut power"
- note added: "led used to show idx activity"
- note added: "use internal pullup of atxmega"
- note removed: "voir si ces éléments ne sont pas a placer sur une carte dédiée avec ventilateur et top tour"
- moved on the sheet: BAL1, C1, C10, C13, C14, C15, C16, C17, C18, C19, C20, C21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
